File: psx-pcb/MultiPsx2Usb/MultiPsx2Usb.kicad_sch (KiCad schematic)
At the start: 1 part

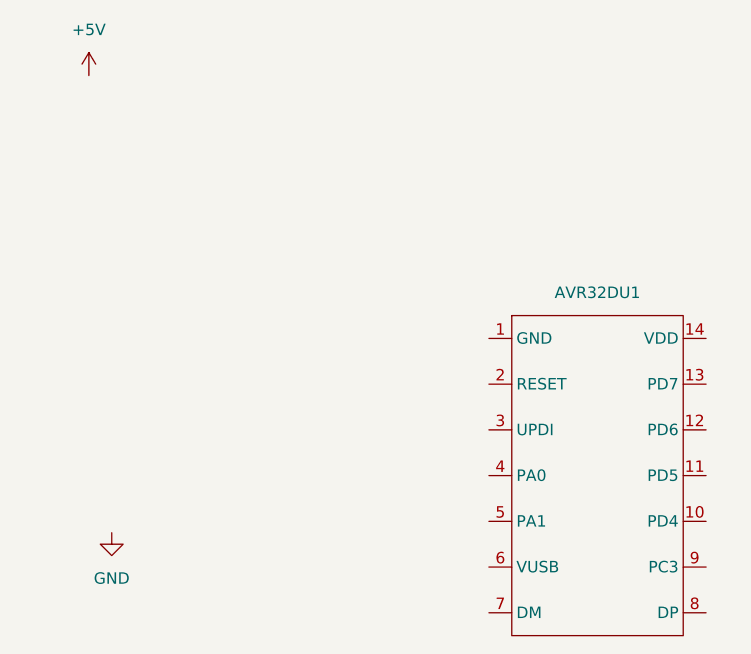
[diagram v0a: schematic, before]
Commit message: Committing latest changes to schematic
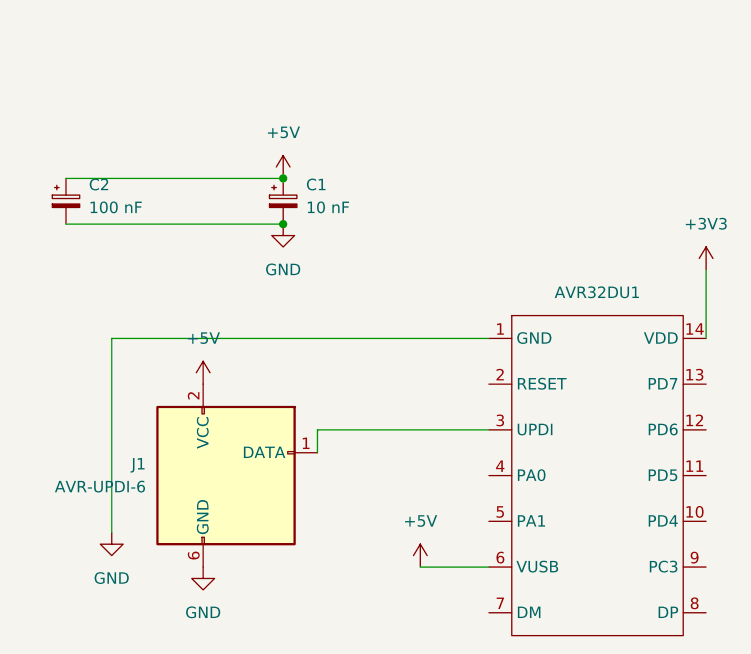
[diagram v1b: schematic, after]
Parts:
- added C1: 10 nF, Capacitor_SMD:C_0603_1608Metric_Pad1.08x0.95mm_HandSolder, symbol Device:C_Polarized_Small
- added C2: 100 nF, Capacitor_SMD:C_0603_1608Metric_Pad1.08x0.95mm_HandSolder, symbol Device:C_Polarized_Small
- added J1: AVR-UPDI-6, symbol Connector:AVR-UPDI-6
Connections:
- net +5V: now also AVR32DU1.6 (VUSB), C1.1, C2.1, J1.2 (VCC)
- net GND: now also AVR32DU1.1 (GND), C1.2, C2.2, J1.6 (GND)
- net +3V3: now reaches AVR32DU1.14 (VDD)
- net at AVR32DU1.3 (UPDI): now also J1.1 (DATA)

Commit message: Rough schematic mockup done. need to create test circuits and see what works and what doesn't.
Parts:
- added C3, C6: 0.1 uF, Capacitor_SMD:C_0603_1608Metric_Pad1.08x0.95mm_HandSolder, symbol Device:C
- added C4: 100 nF, Capacitor_SMD:C_0603_1608Metric_Pad1.08x0.95mm_HandSolder, symbol Device:C
- added C5: 22 uF, Capacitor_SMD:C_0603_1608Metric_Pad1.08x0.95mm_HandSolder, symbol Device:C
- added D1: MBRS120T3G, Diode_SMD:D_SMB_Handsoldering, symbol Device:D_Schottky
- added D2: D_Schottky, symbol Device:D_Schottky
- added J2: USB_C_Receptacle_USB2.0_14P, symbol Connector:USB_C_Receptacle_USB2.0_14P
- added L1: 22 uH, Inductor_SMD:L_0603_1608Metric_Pad1.05x0.95mm_HandSolder, symbol Device:L
- added NCV1: (no value), Package_SO:SOIC-8-1EP_3.9x4.9mm_P1.27mm_EP2.41x3.81mm_ThermalVias, symbol avr32du:NCV5171
- added PS2_CON1: (no value), avr32du:PS2_CONNECTOR, symbol avr32du:PS2_CONNECTOR
- added R1, R2: 5.1k, Resistor_SMD:R_0603_1608Metric_Pad0.98x0.95mm_HandSolder, symbol Device:R
- added R3: 330, Resistor_SMD:R_0603_1608Metric_Pad0.98x0.95mm_HandSolder, symbol Device:R
- added R4: 5K, Resistor_SMD:R_0603_1608Metric_Pad0.98x0.95mm_HandSolder, symbol Device:R
- added R5: 3.72k, Resistor_SMD:R_0603_1608Metric_Pad0.98x0.95mm_HandSolder, symbol Device:R
- added R6: 1.28k, Resistor_SMD:R_0603_1608Metric_Pad0.98x0.95mm_HandSolder, symbol Device:R
- added R7: 1k, Resistor_SMD:R_0603_1608Metric_Pad0.98x0.95mm_HandSolder, symbol Device:R
- added R8: R, Resistor_SMD:R_0603_1608Metric_Pad0.98x0.95mm_HandSolder, symbol Device:R
- added SW1: SW_Push, Button_Switch_SMD:SW_Push_1P1T_XKB_TS-1187A, symbol Switch:SW_Push
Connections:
- net +3V3: now also C1.1, C2.1, J1.2 (VCC), PS2_CON1.5 (PWR), R7.1, R8.1
- net +5V: now also C3.1, J2.A4 (VBUS), J2.A9 (VBUS), J2.B4 (VBUS), J2.B9 (VBUS); no longer C1.1, C2.1, J1.2 (VCC)
- net GND: now also C3.2, C4.2, C5.2, D2.2 (A), J2.A1 (GND), J2.A12 (GND), J2.B1 (GND), J2.B12 (GND), J2.SH (SHIELD), NCV1.6 (PGND), NCV1.7 (AGND), PS2_CON1.4 (GND), R1.2, R2.2, R4.2, R6.2, SW1.2
- net at AVR32DU1.10 (PD4): now also PS2_CON1.2 (COMMAND)
- net at AVR32DU1.11 (PD5): now also PS2_CON1.1 (DATA), R8.2
- net at AVR32DU1.12 (PD6): now also PS2_CON1.7 (CLK)
- net at AVR32DU1.13 (PD7): now also PS2_CON1.6 (ATT)
- net at AVR32DU1.2 (RESET): now also C4.1, R3.1
- net SS: now reaches AVR32DU1.4 (PA0)
- net SS: now also NCV1.4 (SS)
- net at AVR32DU1.7 (DM): now also J2.A7 (D-), J2.B7 (D-)
- net at AVR32DU1.8 (DP): now also J2.A6 (D+), J2.B6 (D+)
- net at AVR32DU1.9 (PC3): now also PS2_CON1.9 (ACK), R7.2
- new net: J2.A5 (CC1), R2.1
- new net: C6.1, NCV1.1 (VC)
- new net: C6.2, R4.1
- new net: NCV1.2 (FB), R5.2, R6.1
- new net: J2.B5 (CC2), R1.1
- new net: D1.2 (A), L1.1, NCV1.8 (V_SW)
- new net: R3.2, SW1.1
- new net +3.3V: C5.1, L1.2, NCV1.5 (V_CC)
- new net +7.5V: D1.1 (K), D2.1 (K), PS2_CON1.3 (VIBRATION), R5.1
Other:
- moved on the sheet: C1, C2, J1
